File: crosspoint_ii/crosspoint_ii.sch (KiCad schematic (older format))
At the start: 1 part, among them P1 DIN_41612_128P

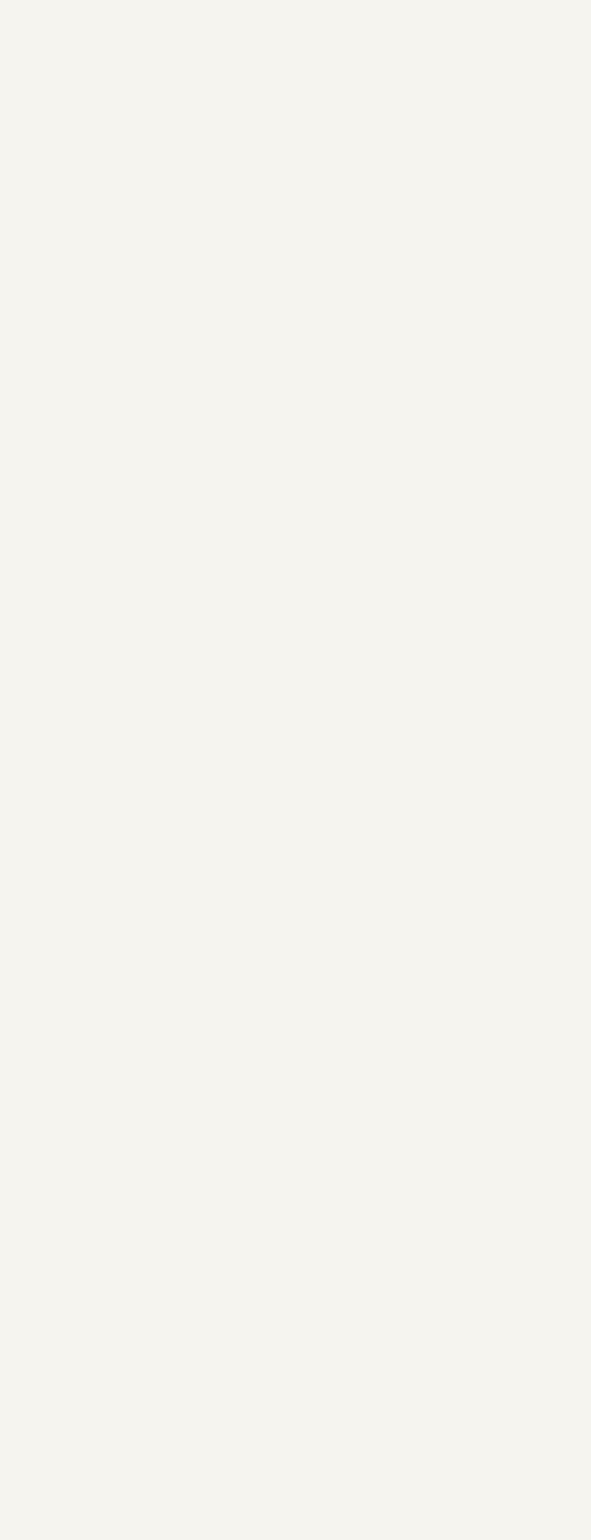
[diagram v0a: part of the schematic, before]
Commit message: Page 2 of module 6, plus a few corrections.
Changed RPTSET in module 3 from an output to an input. Dropped unneeded
pullups from R1C/ (turns out this missing one is in module 6) and RB1/
(I don't remember why that was there) in module 4.
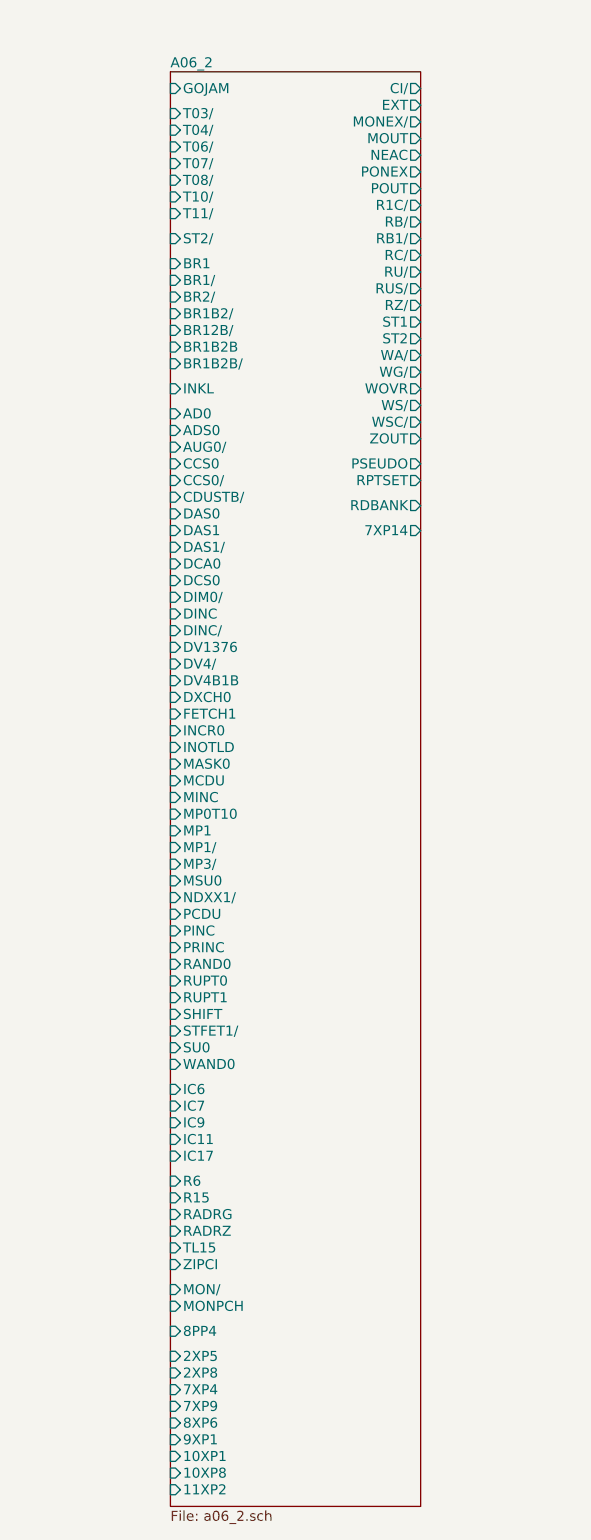
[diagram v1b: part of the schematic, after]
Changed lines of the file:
@@
 $Descr A2 23386 16535
 encoding utf-8
-Sheet 1 2
+Sheet 1 3
 Title ""
 Date ""
@@
 Wire Wire Line
 	15550 2400 15650 2400
+$Sheet
+S 6600 2450 1500 8600
+U 567D63F2
+F0 "A06_2" 60
+F1 "a06_2.sch" 60
+F2 "BR1" I L 6600 3600 60
+F3 "AUG0/" I L 6600 4700 60
+F4 "DIM0/" I L 6600 5600 60
+F5 "BR12B/" I L 6600 4000 60
+F6 "INCR0" I L 6600 6400 60
+F7 "PINC" I L 6600 7600 60
+F8 "DINC/" I L 6600 5800 60
+F9 "T06/" I L 6600 2900 60
+F10 "MINC" I L 6600 6800 60
+F11 "MCDU" I L 6600 6700 60
+F12 "BR1/" I L 6600 3700 60
+F13 "BR1B2B/" I L 6600 4200 60
+F14 "MONEX/" O R 8100 2750 60
+F15 "PCDU" I L 6600 7500 60
+F16 "POUT" O R 8100 3150 60
+F17 "MOUT" O R 8100 2850 60
+F18 "ZOUT" O R 8100 4650 60
+F19 "CDUSTB/" I L 6600 5000 60
+F20 "BR2/" I L 6600 3800 60
+F21 "DAS0" I L 6600 5100 60
+F22 "MSU0" I L 6600 7300 60
+F23 "DAS1" I L 6600 5200 60
+F24 "T07/" I L 6600 3000 60
+F25 "DV4/" I L 6600 6000 60
+F26 "BR1B2B" I L 6600 4100 60
+F27 "WAND0" I L 6600 8400 60
+F28 "RAND0" I L 6600 7800 60
+F29 "WA/" O R 8100 4150 60
+F30 "INOTLD" I L 6600 6500 60
+F31 "7XP14" O R 8100 5200 60
+F32 "DAS1/" I L 6600 5300 60
+F33 "BR1B2/" I L 6600 3900 60
+F34 "RB1/" O R 8100 3450 60
+F35 "R1C/" O R 8100 3250 60
+F36 "SHIFT" I L 6600 8100 60
+F37 "RUS/" O R 8100 3750 60
+F38 "7XP9" I L 6600 10450 60
+F39 "11XP2" I L 6600 10950 60
+F40 "PRINC" I L 6600 7700 60
+F41 "DINC" I L 6600 5700 60
+F42 "RU/" O R 8100 3650 60
+F43 "INKL" I L 6600 4350 60
+F44 "MONPCH" I L 6600 9850 60
+F45 "T04/" I L 6600 2800 60
+F46 "MON/" I L 6600 9750 60
+F47 "FETCH1" I L 6600 6300 60
+F48 "WOVR" O R 8100 4350 60
+F49 "WSC/" O R 8100 4550 60
+F50 "WG/" O R 8100 4250 60
+F51 "IC9" I L 6600 8750 60
+F52 "DXCH0" I L 6600 6200 60
+F53 "RB/" O R 8100 3350 60
+F54 "RUPT1" I L 6600 8000 60
+F55 "8PP4" I L 6600 10000 60
+F56 "IC17" I L 6600 8950 60
+F57 "MASK0" I L 6600 6600 60
+F58 "IC11" I L 6600 8850 60
+F59 "IC6" I L 6600 8550 60
+F60 "IC7" I L 6600 8650 60
+F61 "DV4B1B" I L 6600 6100 60
+F62 "T08/" I L 6600 3100 60
+F63 "RUPT0" I L 6600 7900 60
+F64 "MP1" I L 6600 7000 60
+F65 "DV1376" I L 6600 5900 60
+F66 "WS/" O R 8100 4450 60
+F67 "R6" I L 6600 9100 60
+F68 "R15" I L 6600 9200 60
+F69 "MP3/" I L 6600 7200 60
+F70 "CCS0" I L 6600 4800 60
+F71 "T11/" I L 6600 3300 60
+F72 "ADS0" I L 6600 4600 60
+F73 "T03/" I L 6600 2700 60
+F74 "8XP6" I L 6600 10550 60
+F75 "7XP4" I L 6600 10350 60
+F76 "10XP8" I L 6600 10850 60
+F77 "PONEX" O R 8100 3050 60
+F78 "ZIPCI" I L 6600 9600 60
+F79 "CI/" O R 8100 2550 60
+F80 "DCA0" I L 6600 5400 60
+F81 "AD0" I L 6600 4500 60
+F82 "CCS0/" I L 6600 4900 60
+F83 "T10/" I L 6600 3200 60
+F84 "NDXX1/" I L 6600 7400 60
+F85 "EXT" O R 8100 2650 60
+F86 "2XP5" I L 6600 10150 60
+F87 "DCS0" I L 6600 5500 60
+F88 "SU0" I L 6600 8300 60
+F89 "RC/" O R 8100 3550 60
+F90 "MP1/" I L 6600 7100 60
+F91 "RADRZ" I L 6600 9400 60
+F92 "ST2" O R 8100 4050 60
+F93 "ST2/" I L 6600 3450 60
+F94 "2XP8" I L 6600 10250 60
+F95 "10XP1" I L 6600 10750 60
+F96 "MP0T10" I L 6600 6900 60
+F97 "ST1" O R 8100 3950 60
+F98 "RZ/" O R 8100 3850 60
+F99 "9XP1" I L 6600 10650 60
+F100 "NEAC" O R 8100 2950 60
+F101 "TL15" I L 6600 9500 60
+F102 "GOJAM" I L 6600 2550 60
+F103 "RADRG" I L 6600 9300 60
+F104 "PSEUDO" O R 8100 4800 60
+F105 "RPTSET" O R 8100 4900 60
+F106 "STFET1/" I L 6600 8200 60
+F107 "RDBANK" O R 8100 5050 60
+$EndSheet
 $EndSCHEMATC

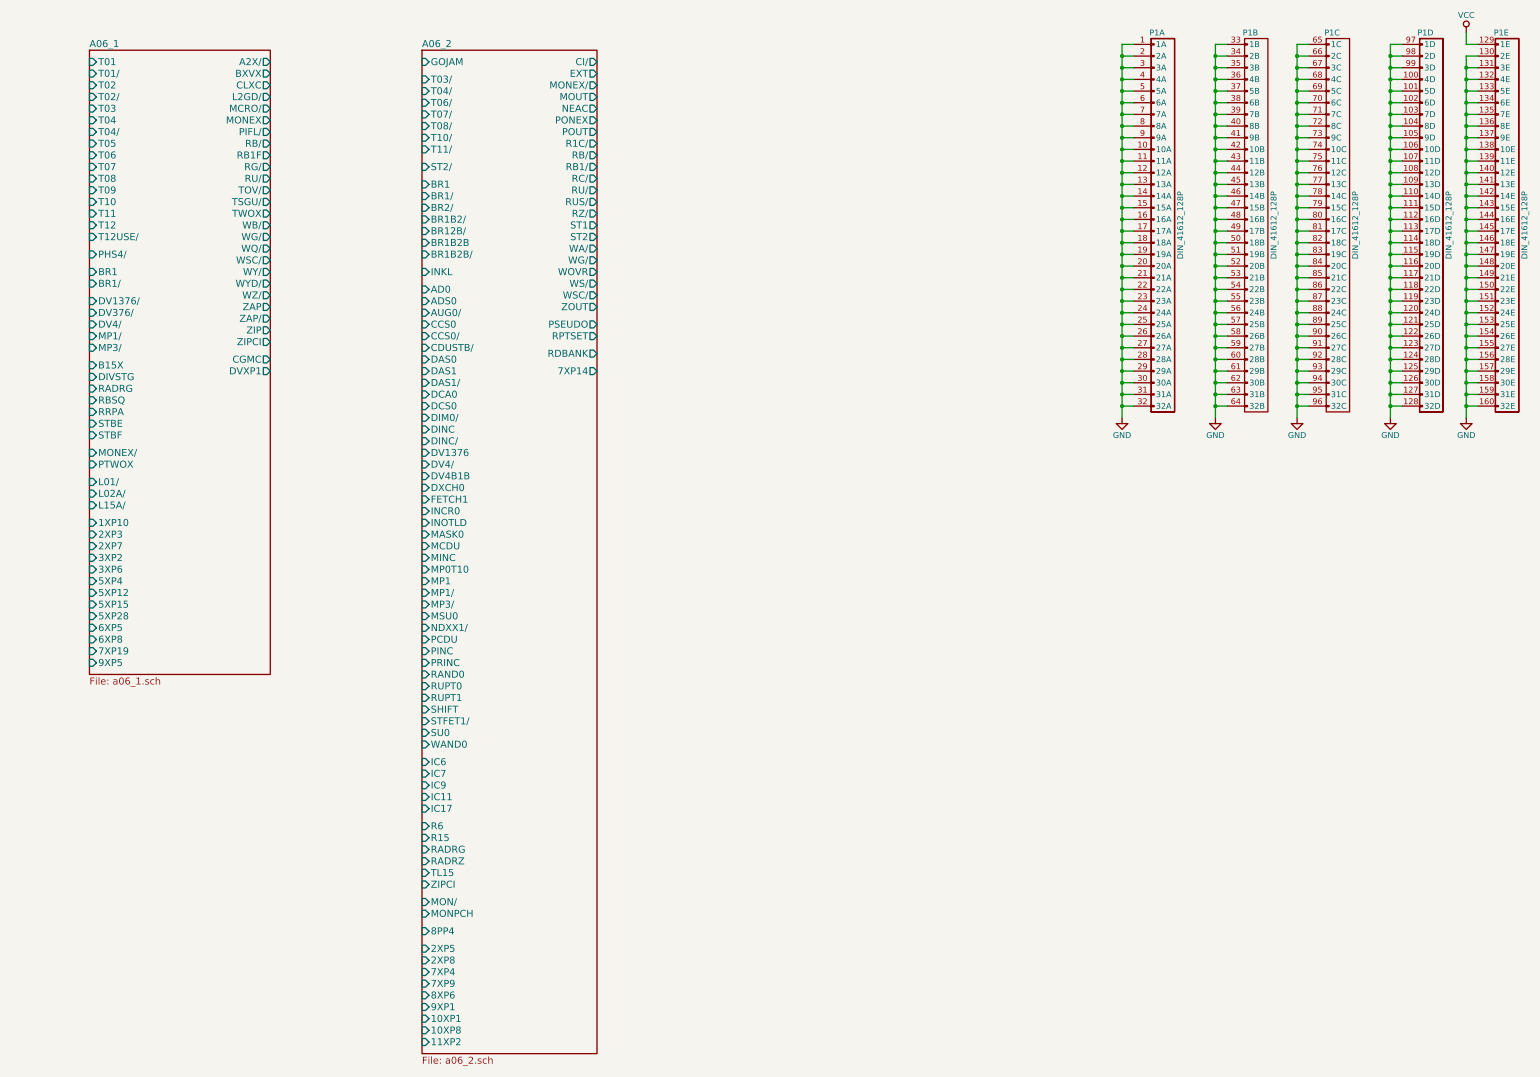
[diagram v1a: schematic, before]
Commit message: Tied in module 6 and corrected a handful of naming/routing errors... most notably some missing gates from A06-1
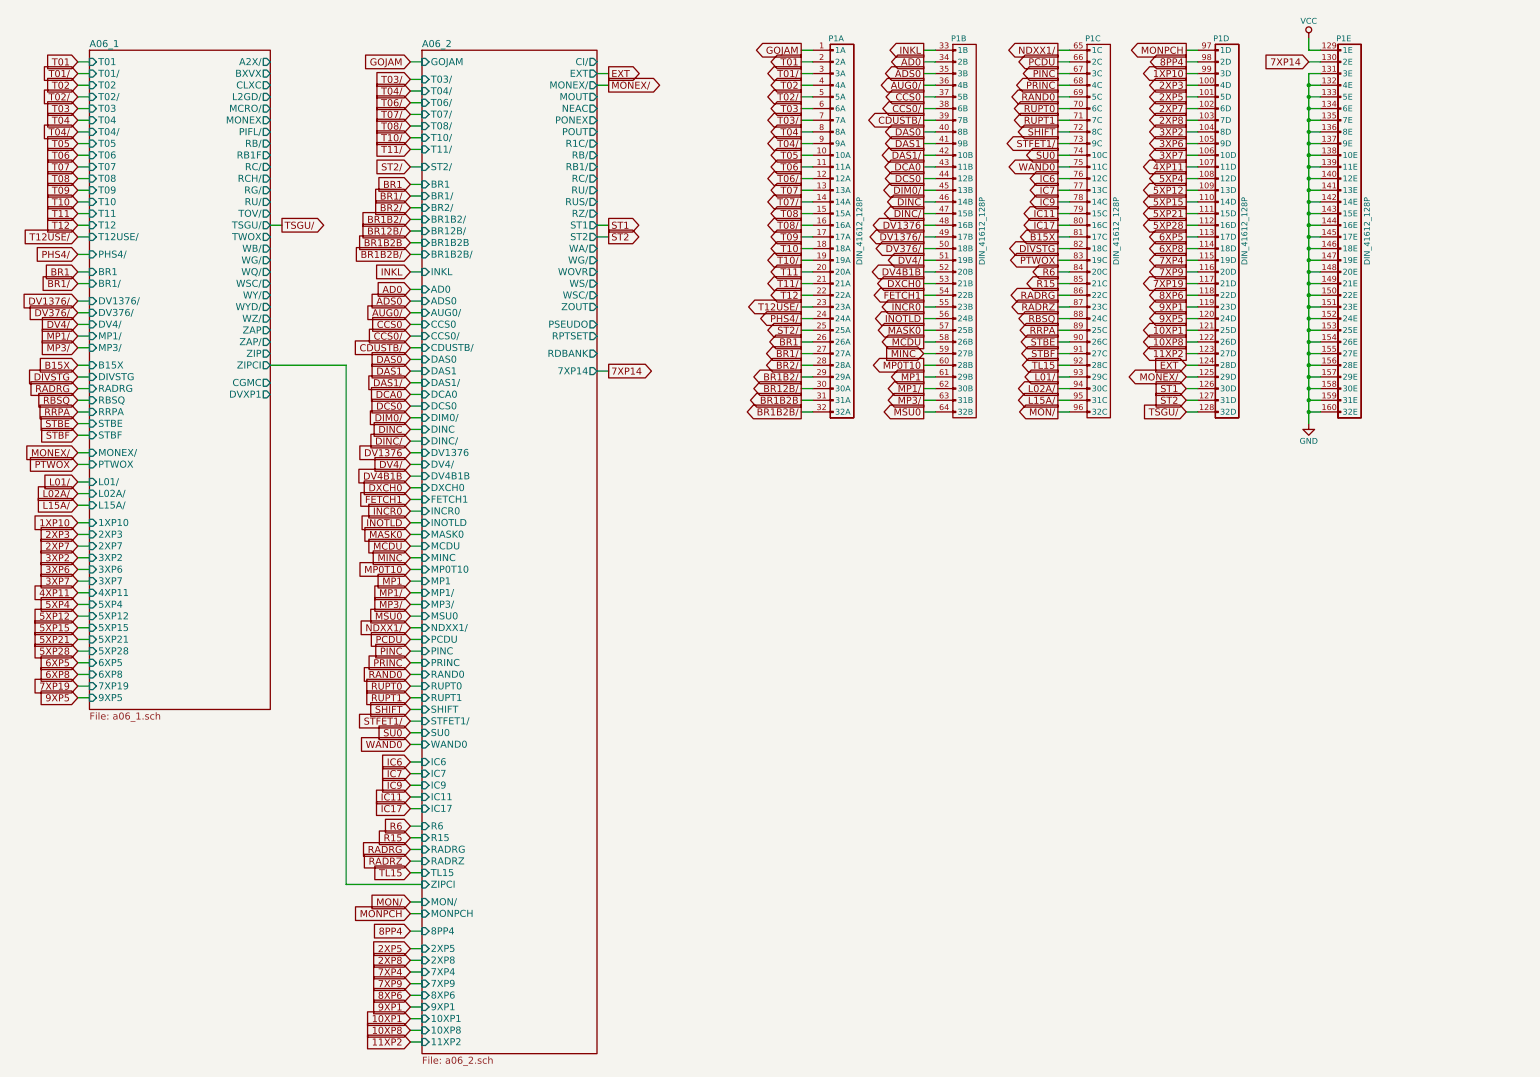
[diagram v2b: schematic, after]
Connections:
- net GND: no longer P1.1 (1A), P1.10 (10A), P1.100 (4D), P1.101 (5D), P1.102 (6D), P1.103 (7D), P1.104 (8D), P1.105 (9D), P1.106 (10D), P1.107 (11D), P1.108 (12D), P1.109 (13D), P1.11 (11A), P1.110 (14D), P1.111 (15D), P1.112 (16D), P1.113 (17D), P1.114 (18D), P1.115 (19D), P1.116 (20D), P1.117 (21D), P1.118 (22D), P1.119 (23D), P1.12 (12A), P1.120 (24D), P1.121 (25D), P1.122 (26D), P1.123 (27D), P1.124 (28D), P1.125 (29D), P1.126 (30D), P1.127 (31D), P1.128 (32D), P1.13 (13A), P1.130 (2E), P1.14 (14A), P1.15 (15A), P1.16 (16A), P1.17 (17A), P1.18 (18A), P1.19 (19A), P1.2 (2A), P1.20 (20A), P1.21 (21A), P1.22 (22A), P1.23 (23A), P1.24 (24A), P1.25 (25A), P1.26 (26A), P1.27 (27A), P1.28 (28A), P1.29 (29A), P1.3 (3A), P1.30 (30A), P1.31 (31A), P1.32 (32A), P1.33 (1B), P1.34 (2B), P1.35 (3B), P1.36 (4B), P1.37 (5B), P1.38 (6B), P1.39 (7B), P1.4 (4A), P1.40 (8B), P1.41 (9B), P1.42 (10B), P1.43 (11B), P1.44 (12B), P1.45 (13B), P1.46 (14B), P1.47 (15B), P1.48 (16B), P1.49 (17B), P1.5 (5A), P1.50 (18B), P1.51 (19B), P1.52 (20B), P1.53 (21B), P1.54 (22B), P1.55 (23B), P1.56 (24B), P1.57 (25B), P1.58 (26B), P1.59 (27B), P1.6 (6A), P1.60 (28B), P1.61 (29B), P1.62 (30B), P1.63 (31B), P1.64 (32B), P1.65 (1C), P1.66 (2C), P1.67 (3C), P1.68 (4C), P1.69 (5C), P1.7 (7A), P1.70 (6C), P1.71 (7C), P1.72 (8C), P1.73 (9C), P1.74 (10C), P1.75 (11C), P1.76 (12C), P1.77 (13C), P1.78 (14C), P1.79 (15C), P1.8 (8A), P1.80 (16C), P1.81 (17C), P1.82 (18C), P1.83 (19C), P1.84 (20C), P1.85 (21C), P1.86 (22C), P1.87 (23C), P1.88 (24C), P1.89 (25C), P1.9 (9A), P1.90 (26C), P1.91 (27C), P1.92 (28C), P1.93 (29C), P1.94 (30C), P1.95 (31C), P1.96 (32C), P1.97 (1D), P1.98 (2D), P1.99 (3D)
- new net 10XP1: P1.121 (25D)
- new net 10XP8: P1.122 (26D)
- new net 11XP2: P1.123 (27D)
- new net 1XP10: P1.99 (3D)
- new net 2XP3: P1.100 (4D)
- new net 2XP5: P1.101 (5D)
- new net 2XP7: P1.102 (6D)
- new net 2XP8: P1.103 (7D)
- new net 3XP2: P1.104 (8D)
- new net 3XP6: P1.105 (9D)
- new net 3XP7: P1.106 (10D)
- new net 4XP11: P1.107 (11D)
- new net 5XP12: P1.109 (13D)
- new net 5XP15: P1.110 (14D)
- new net 5XP21: P1.111 (15D)
- new net 5XP28: P1.112 (16D)
- new net 5XP4: P1.108 (12D)
- new net 6XP5: P1.113 (17D)
- new net 6XP8: P1.114 (18D)
- new net 7XP14: P1.130 (2E)
- new net 7XP19: P1.117 (21D)
- new net 7XP4: P1.115 (19D)
- new net 7XP9: P1.116 (20D)
- new net 8PP4: P1.98 (2D)
- new net 8XP6: P1.118 (22D)
- new net 9XP1: P1.119 (23D)
- new net 9XP5: P1.120 (24D)
- new net AD0: P1.34 (2B)
- new net ADS0: P1.35 (3B)
- new net AUG0/: P1.36 (4B)
- new net B15X: P1.81 (17C)
- new net BR1: P1.26 (26A)
- new net BR1/: P1.27 (27A)
- new net BR12B/: P1.30 (30A)
- new net BR1B2/: P1.29 (29A)
- new net BR1B2B: P1.31 (31A)
- new net BR1B2B/: P1.32 (32A)
- new net BR2/: P1.28 (28A)
- new net CCS0: P1.37 (5B)
- new net CCS0/: P1.38 (6B)
- new net CDUSTB/: P1.39 (7B)
- new net DAS0: P1.40 (8B)
- new net DAS1: P1.41 (9B)
- new net DAS1/: P1.42 (10B)
- new net DCA0: P1.43 (11B)
- new net DCS0: P1.44 (12B)
- new net DIM0/: P1.45 (13B)
- new net DINC: P1.46 (14B)
- new net DINC/: P1.47 (15B)
- new net DIVSTG: P1.82 (18C)
- new net DV1376: P1.48 (16B)
- new net DV1376/: P1.49 (17B)
- new net DV376/: P1.50 (18B)
- new net DV4/: P1.51 (19B)
- new net DV4B1B: P1.52 (20B)
- new net DXCH0: P1.53 (21B)
- new net EXT: P1.124 (28D)
- new net FETCH1: P1.54 (22B)
- new net GOJAM: P1.1 (1A)
- new net IC11: P1.79 (15C)
- new net IC17: P1.80 (16C)
- new net IC6: P1.76 (12C)
- new net IC7: P1.77 (13C)
- new net IC9: P1.78 (14C)
- new net INCR0: P1.55 (23B)
- new net INKL: P1.33 (1B)
- new net INOTLD: P1.56 (24B)
- new net L01/: P1.93 (29C)
- new net L02A/: P1.94 (30C)
- new net L15A/: P1.95 (31C)
- new net MASK0: P1.57 (25B)
- new net MCDU: P1.58 (26B)
- new net MINC: P1.59 (27B)
- new net MON/: P1.96 (32C)
- new net MONEX/: P1.125 (29D)
- new net MONPCH: P1.97 (1D)
- new net MP0T10: P1.60 (28B)
- new net MP1: P1.61 (29B)
- new net MP1/: P1.62 (30B)
- new net MP3/: P1.63 (31B)
- new net MSU0: P1.64 (32B)
- new net NDXX1/: P1.65 (1C)
- new net PCDU: P1.66 (2C)
- new net PHS4/: P1.24 (24A)
- new net PINC: P1.67 (3C)
- new net PRINC: P1.68 (4C)
- new net PTWOX: P1.83 (19C)
- new net R15: P1.85 (21C)
- new net R6: P1.84 (20C)
- new net RADRG: P1.86 (22C)
- new net RADRZ: P1.87 (23C)
- new net RAND0: P1.69 (5C)
- new net RBSQ: P1.88 (24C)
- new net RRPA: P1.89 (25C)
- new net RUPT0: P1.70 (6C)
- new net RUPT1: P1.71 (7C)
- new net SHIFT: P1.72 (8C)
- new net ST1: P1.126 (30D)
- new net ST2: P1.127 (31D)
- new net ST2/: P1.25 (25A)
- new net STBE: P1.90 (26C)
- new net STBF: P1.91 (27C)
- new net STFET1/: P1.73 (9C)
- new net SU0: P1.74 (10C)
- new net T01: P1.2 (2A)
- new net T01/: P1.3 (3A)
- new net T02: P1.4 (4A)
- new net T02/: P1.5 (5A)
- new net T03: P1.6 (6A)
- new net T03/: P1.7 (7A)
- new net T04: P1.8 (8A)
- new net T04/: P1.9 (9A)
- new net T05: P1.10 (10A)
- new net T06: P1.11 (11A)
- new net T06/: P1.12 (12A)
- new net T07: P1.13 (13A)
- new net T07/: P1.14 (14A)
- new net T08: P1.15 (15A)
- new net T08/: P1.16 (16A)
- new net T09: P1.17 (17A)
- new net T10: P1.18 (18A)
- new net T10/: P1.19 (19A)
- new net T11: P1.20 (20A)
- new net T11/: P1.21 (21A)
- new net T12: P1.22 (22A)
- new net T12USE/: P1.23 (23A)
- new net TL15: P1.92 (28C)
- new net TSGU/: P1.128 (32D)
- new net WAND0: P1.75 (11C)
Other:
- moved on the sheet: P1A, P1B, P1C, P1D, P1E

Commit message: Broke out some open drain signals that were only partially onto the backplane... I missed them because inouts are sufficient to satisfy an input criterion, so there's no error if only part of the signal is on the backplane. Will keep an eye on inouts...
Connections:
- net 7XP14: now also P1.132 (4E); no longer P1.130 (2E)
- net GND: no longer P1.131 (3E), P1.132 (4E)
- net TSGU/: now also P1.130 (2E); no longer P1.128 (32D)
- new net RPTSET: P1.131 (3E)
- new net TOV/: P1.128 (32D)
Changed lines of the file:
@@
 	14200 2850 14300 2850
 Connection ~ 14200 2950
-Wire Wire Line
-	14200 2750 14300 2750
-Connection ~ 14200 2850
-Wire Wire Line
-	14200 2650 14300 2650
-Connection ~ 14200 2750
 $Comp
 L VCC #PWR02
@@
 Wire Wire Line
 	5400 3950 5300 3950
-Text GLabel 13150 5550 0    60   Input ~ 0
+Text GLabel 14200 2550 0    60   Input ~ 0
 TSGU/
 Wire Wire Line
-	13150 5550 13250 5550
+	14200 2550 14300 2550
 Text GLabel 3650 7000 0    60   Input ~ 0
 3XP7
@@
 Wire Wire Line
 	8200 5200 8100 5200
-Wire Wire Line
-	14200 2650 14200 5650
-Text GLabel 14200 2550 0    60   Input ~ 0
+Text GLabel 14200 2750 0    60   Input ~ 0
 7XP14
 Wire Wire Line
-	14200 2550 14300 2550
+	14200 2750 14300 2750
+Text GLabel 8200 4900 2    60   Output ~ 0
+RPTSET
+Wire Wire Line
+	8200 4900 8100 4900
+Text GLabel 14200 2650 0    60   Input ~ 0
+RPTSET
+Wire Wire Line
+	14200 2650 14300 2650
+Text GLabel 5400 3850 2    60   Output ~ 0
+TOV/
+Wire Wire Line
+	5400 3850 5300 3850
+Wire Wire Line
+	14200 2850 14200 5650
+Text GLabel 13150 5550 0    60   Input ~ 0
+TOV/
+Wire Wire Line
+	13150 5550 13250 5550
 $EndSCHEMATC
